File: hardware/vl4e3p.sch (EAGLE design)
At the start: 43 parts, among them Q1 AO3401A

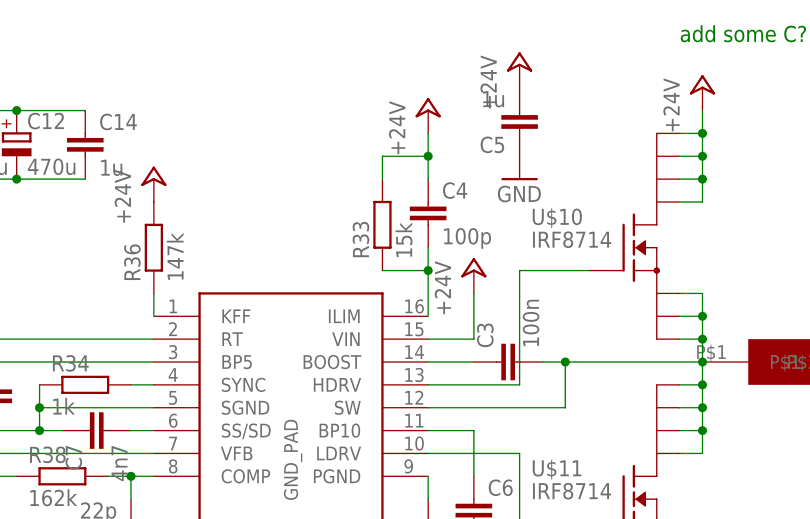
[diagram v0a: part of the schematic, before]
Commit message: hardware: increase current limit of stepdown
The old resistor value was based on a very tightly calculated current
limit and was also rounded down to match an E12 value. This caused some
aging Vaporlights to fail when drawing more current (e.g. displaying all
white).
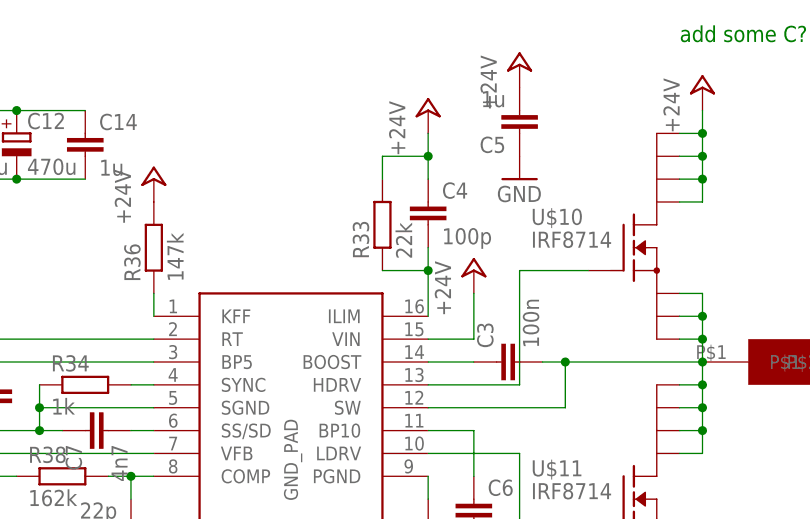
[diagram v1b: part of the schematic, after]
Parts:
- R33: value 15k -> 22k
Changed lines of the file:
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@@
 <part name="GND14" library="supply1" deviceset="GND" device=""/>
 <part name="C4" library="rcl" deviceset="C-EU" device="C0805" value="100p"/>
-<part name="R33" library="rcl" deviceset="R-EU_" device="R0805" value="15k"/>
+<part name="R33" library="rcl" deviceset="R-EU_" device="R0805" value="22k"/>
 <part name="P+7" library="supply1" deviceset="+24V" device=""/>
 <part name="P+8" library="supply1" deviceset="+24V" device=""/>
